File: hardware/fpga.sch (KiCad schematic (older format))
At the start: 18 parts

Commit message: more work on tdr schematic
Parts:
- removed U?: pkl_memory:W25Q, symbol icebreaker-cache:pkl_memory_W25Q
- added C? (x2): 100 nF, symbol Device:C_Small
- added C?: 10 nF, symbol Device:C_Small
- added C?: 2.2 uF, symbol Device:C_Small
- added C?: 100 pF, symbol Device:C_Small
- added L?: L_Small, symbol Device:L_Small
- U? (x4): symbol synth_lib:ICE40UP5K-SG48ITR -> tdr-rescue:ICE40UP5K-SG48ITR-synth_lib
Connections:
- net labels added: DELAY_SCLK, DELAY_SDIN, DELAY_SLOAD, DELAY_~EN, SEL0, SEL1, TRIG_DAC_CS, TRIG_DAC_SCK, TRIG_DAC_SDI
- net labels removed: D0_PULSE, D0_SAMPLE, D1_PULSE, D1_SAMPLE, D2_PULSE, D2_SAMPLE, D3_PULSE, D3_SAMPLE, D4_PULSE, D4_SAMPLE, D5_PULSE, D5_SAMPLE, D6_PULSE, D6_SAMPLE, D7_PULSE, D7_SAMPLE, D8_PULSE, D8_SAMPLE, D9_PULSE, D9_SAMPLE, PULSE_LATCH, SAMPLE_LATCH, ~PULSE_EN, ~SAMPLE_EN
- wire segments 72 -> 94
- no-connect marks 7 -> 0
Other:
- note added: "TODO: add digital test/ext control headers"
- note removed: "TODO: TERMINATE THESE"
- moved on the sheet: C?, R?

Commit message: work on tdr schematic..
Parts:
- removed C? (x5): 100 nF, symbol Device:C_Small
- removed C? (x3): 100 pF, symbol Device:C_Small
- removed C?: 10 uF, symbol Device:C_Small
- removed C? (x3): 10 nF, symbol Device:C_Small
- removed C? (x2): 1 uF, symbol Device:C_Small
- removed C?: 2.2 uF, symbol Device:C_Small
- removed L?: L_Small, symbol Device:L_Small
- removed R? (x3): R_Small, symbol Device:R_Small
- removed U? (x4): ICE40UP5K-SG48ITR, Package_DFN_QFN:QFN-48-1EP_7x7mm_P0.5mm_EP5.6x5.6mm, symbol tdr-rescue:ICE40UP5K-SG48ITR-synth_lib
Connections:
- net labels added: DAC_CS, DAC_SCK, DAC_SDI
- net labels removed: +1V2, +2V5, +3.3VP, +3V3, D0_DAC, D1_DAC, D2_DAC, D3_DAC, D4_DAC, D5_DAC, D6_DAC, D7_DAC, D8_DAC, D9_DAC, DAC_SLEEP, FLASH_~HLD~|~RST, FLASH_~WP, GND, ICE_DONE, ICE_SCK, ICE_SI, ICE_SO, ICE_SS, ICE_~RESET, TRIG_DAC_CS, TRIG_DAC_SCK, TRIG_DAC_SDI, UART_RX, UART_TX
- wire segments 94 -> 0
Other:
- note removed: "TODO: OPEN COLLECTOR!"

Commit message: work on schematic..
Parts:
- added C801, C803, C805, C807, C811, C812, C813, C814, C815, C816, C817, C818, C819, C820, C821, C822: 33 pF, Capacitors_SMD:C_0402, symbol Device:C_Small
- added C802, C806: 1 uF, Capacitors_SMD:C_0603, symbol Device:C_Small
- added C804, C808: 10 nF, Capacitors_SMD:C_0402, symbol Device:C_Small
- added C809, C810: C_Small, Capacitors_SMD:C_0402, symbol Device:C_Small
- added J801, J802: Conn_02x06_Odd_Even, Pin_Headers:Pin_Header_Angled_2x06, symbol Connector_Generic:Conn_02x06_Odd_Even
- added L801, L802: L_Small, Resistors_SMD:R_0402, symbol Device:L_Small
- added RN801, RN802, RN803, RN804, RN805, RN806, RN807: 22, Resistors_SMD:R_Array_Convex_4x0402, symbol Device:R_Pack04
- added TP801, TP802, TP803: TestPoint, vna_footprints:TP07R, symbol Connector:TestPoint
- added U801, U802: 74HC244, Housings_SSOP:TSSOP-20_4.4x6.5mm_Pitch0.65mm, symbol 74xx:74HC244
- added U803: 74xx1G14, TO_SOT_Packages_SMD:SOT-23-5, symbol 74xx1g14:74xx1G14
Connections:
- net DAC_CS: now also C821.1, RN807.7 (R2.2)
- net DAC_SCK: now also C819.1, RN807.6 (R3.2)
- net DAC_SDI: now also C817.1, RN807.5 (R4.2)
- net DELAY_SCLK: now also C816.1, RN806.6 (R3.2)
- net DELAY_SDIN: now also C818.1, RN806.7 (R2.2)
- net DELAY_SLOAD: now also C811.1, RN803.5 (R4.2)
- net DELAY_~EN: now also C815.1, RN806.5 (R4.2)
- net FPGA_CLK: now also C801.1, RN801.8 (R1.2)
- net REF_CLK_SEL: now also C812.1, RN803.6 (R3.2)
- net SEL0: now also C813.1, RN803.7 (R2.2)
- net SEL1: now also C814.1, RN803.8 (R1.2)
- new net: U801.1 (1OE), U802.1 (1OE), U802.19 (2OE), U803.4 (Y)
- new net: RN805.5 (R4.2), U802.11 (2A3)
- new net: RN807.4 (R4.1), U802.12 (1Y3)
- new net: RN805.6 (R3.2), U802.13 (2A2)
- new net: RN807.3 (R3.1), U802.14 (1Y2)
- new net: RN805.7 (R2.2), U802.15 (2A1)
- new net: RN807.2 (R2.1), U802.16 (1Y1)
- new net: RN805.8 (R1.2), U802.17 (2A0)
- new net: RN807.1 (R1.1), U802.18 (1Y0)
- new net: RN804.8 (R1.2), U802.2 (1A0)
- new net: C806.1, C808.1, L802.2, U802.20 (VCC)
- new net: RN803.1 (R1.1), U802.3 (2Y0)
- new net: RN804.7 (R2.2), U802.4 (1A1)
- new net: RN803.2 (R2.1), U802.5 (2Y1)
- new net: RN804.6 (R3.2), U802.6 (1A2)
- new net: RN803.3 (R3.1), U802.7 (2Y2)
- new net: RN804.5 (R4.2), U802.8 (1A3)
- new net: RN803.4 (R4.1), U802.9 (2Y3)
- new net: J801.1 (Pin_1), RN801.1 (R1.1)
- new net: J801.3 (Pin_3), RN801.2 (R2.1)
- new net: J801.5 (Pin_5), RN801.3 (R3.1)
- new net: J801.7 (Pin_7), RN801.4 (R4.1)
- new net: C807.1, RN801.5 (R4.2), TP803.1
- new net: C805.1, RN801.6 (R3.2), TP802.1
- new net: C803.1, RN801.7 (R2.2), TP801.1
- new net: RN806.4 (R4.1), U801.12 (1Y3)
- new net: RN806.3 (R3.1), U801.14 (1Y2)
- new net: RN806.2 (R2.1), U801.16 (1Y1)
- new net: RN806.1 (R1.1), U801.18 (1Y0)
- new net: C802.1, C804.1, L801.2, U801.20 (VCC)
- new net: J802.7 (Pin_7), RN802.5 (R4.2)
- new net: J802.5 (Pin_5), RN802.6 (R3.2)
- new net: J802.3 (Pin_3), RN802.7 (R2.2)
- new net: J802.1 (Pin_1), RN802.8 (R1.2)
- new net: J801.2 (Pin_2), RN804.1 (R1.1)
- new net: J801.4 (Pin_4), RN804.2 (R2.1)
- new net: J801.6 (Pin_6), RN804.3 (R3.1)
- new net: J801.8 (Pin_8), RN804.4 (R4.1)
- new net: J802.2 (Pin_2), RN805.1 (R1.1)
- new net: J802.4 (Pin_4), RN805.2 (R2.1)
- new net: J802.6 (Pin_6), RN805.3 (R3.1)
- new net: J802.8 (Pin_8), RN805.4 (R4.1)
- new net +3.3VP: C809.1, C810.1, J801.11 (Pin_11), J801.12 (Pin_12), J802.11 (Pin_11), J802.12 (Pin_12)
- new net +3V3: L801.1, L802.1, U801.19 (2OE), U803.5 (Vcc)
- new net COMPARATOR_OUTPUT: U801.2 (1A0)
- new net DAC_~CLR: C822.1, RN807.8 (R1.2)
- new net EXT_COMP_OUT: C820.1, RN802.1 (R1.1), RN806.8 (R1.2)
- new net EXT_DELAY_SCK: RN802.4 (R4.1), U801.8 (1A3)
- new net EXT_DELAY_SDIN: RN802.2 (R2.1), U801.4 (1A1)
- new net EXT_DELAY_~EN: RN802.3 (R3.1), U801.6 (1A2)
- new net GND: C801.2, C802.2, C803.2, C804.2, C805.2, C806.2, C807.2, C808.2, C809.2, C810.2, C811.2, C812.2, C813.2, C814.2, C815.2, C816.2, C817.2, C818.2, C819.2, C820.2, C821.2, C822.2, J801.10 (Pin_10), J801.9 (Pin_9), J802.10 (Pin_10), J802.9 (Pin_9), U801.10 (GND), U801.11 (2A3), U801.13 (2A2), U801.15 (2A1), U801.17 (2A0), U802.10 (GND), U803.3 (GND)
- new net PGOOD_3V3: U803.2 (A)
- no-connect marks 0 -> 4
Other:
- note added: "10.16 mm pad center to pad center"
- note added: "7 8 9 0 1 2\n1 2 3 4 5 6"
- note added: "TODO: BUFFER DIGITAL LINES VIA PGOOD SIGNAL OF DIGITAL CHIPS"
- note removed: "TODO: add digital test/ext control headers"

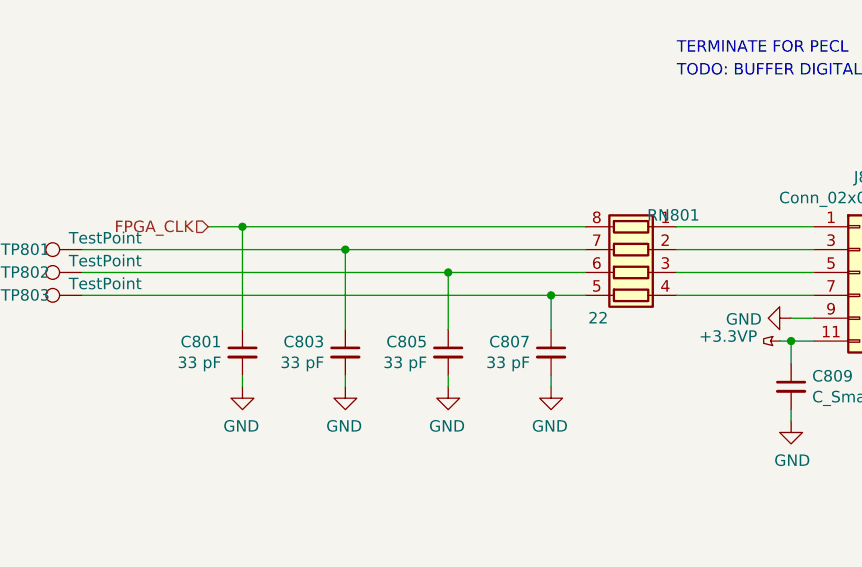
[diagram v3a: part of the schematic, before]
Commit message: work on tdr component placement
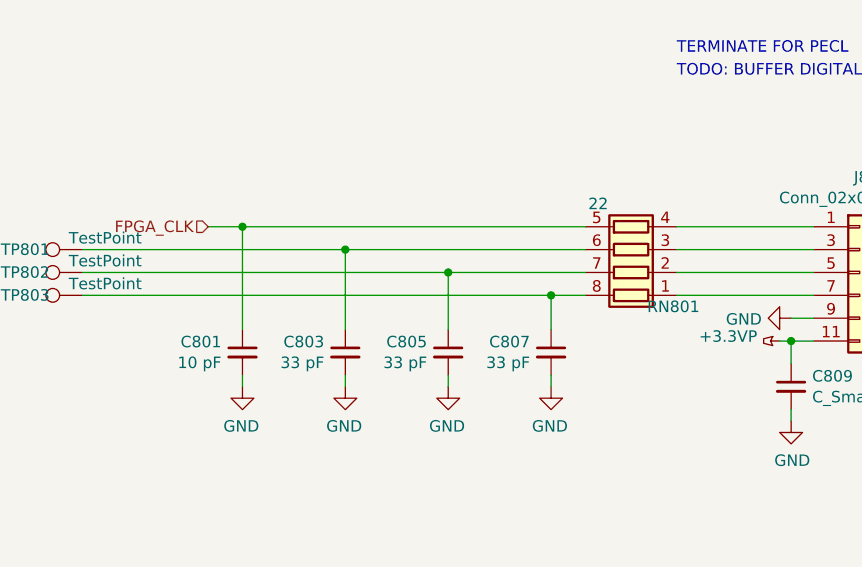
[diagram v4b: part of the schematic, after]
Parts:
- C801: value 33 pF -> 10 pF
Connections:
- net FPGA_CLK: now also RN801.5 (R4.2); no longer RN801.8 (R1.2)
- net at RN801.1 (R1.1): now also J801.7 (Pin_7); no longer J801.1 (Pin_1)
- net at RN801.2 (R2.1): now also J801.5 (Pin_5); no longer J801.3 (Pin_3)
- net at RN801.3 (R3.1): now also J801.3 (Pin_3); no longer J801.5 (Pin_5)
- net at RN801.4 (R4.1): now also J801.1 (Pin_1); no longer J801.7 (Pin_7)
- net at C807.1, TP803.1: now also RN801.8 (R1.2); no longer RN801.5 (R4.2)
- net at C805.1, TP802.1: now also RN801.7 (R2.2); no longer RN801.6 (R3.2)
- net at C803.1, TP801.1: now also RN801.6 (R3.2); no longer RN801.7 (R2.2)
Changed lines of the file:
@@
 L Device:R_Pack04 RN?
 U 1 1 5C12A862
-P 4500 2450
+P 4500 2350
 AR Path="/5BC6A656/5C12A862" Ref="RN?"  Part="1"
 AR Path="/5BC64E97/5C12A862" Ref="RN?"  Part="1"
 AR Path="/5BC3F67C/5C12A862" Ref="RN801"  Part="1"
-F 0 "RN801" V 4250 2150 50  0000 L CNN
-F 1 "22" V 4700 2550 50  0000 L CNN
-F 2 "Resistors_SMD:R_Array_Convex_4x0402" V 4775 2450 50  0001 C CNN
-F 3 "~" H 4500 2450 50  0001 C CNN
-	1    4500 2450
-	0    -1   1    0
+F 0 "RN801" V 4250 2050 50  0000 L CNN
+F 1 "22" V 4700 2450 50  0000 L CNN
+F 2 "Resistors_SMD:R_Array_Convex_4x0402" V 4775 2350 50  0001 C CNN
+F 3 "~" H 4500 2350 50  0001 C CNN
+	1    4500 2350
+	0    -1   -1   0
 $EndComp
 $Comp
@@
 P 2800 2800
 F 0 "C801" H 2892 2846 50  0000 L CNN
-F 1 "33 pF" H 2892 2755 50  0000 L CNN
+F 1 "10 pF" H 2892 2755 50  0000 L CNN
 F 2 "Capacitors_SMD:C_0402" H 2800 2800 50  0001 C CNN
 F 3 "~" H 2800 2800 50  0001 C CNN

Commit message: finished first pass component placement and drc setup, swapped digital pins for easier routing
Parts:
- removed J801, J802: Conn_02x06_Odd_Even, Pin_Headers:Pin_Header_Angled_2x06, symbol Connector_Generic:Conn_02x06_Odd_Even
- added J801, J802: Conn_02x06_Counter_Clockwise, Pin_Headers:Pin_Header_Angled_2x06, symbol Connector_Generic:Conn_02x06_Counter_Clockwise
- C809, C810: value C_Small -> 100 nF
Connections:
- net +3.3VP: now also J801.1 (Pin_1), J801.2 (Pin_2), J802.1 (Pin_1), J802.2 (Pin_2)
- net DELAY_SLOAD: now also RN803.8 (R1.2); no longer RN803.5 (R4.2)
- net EXT_COMP_OUT: now also J802.5 (Pin_5); no longer RN802.1 (R1.1)
- net EXT_DELAY_SCK: now also RN802.1 (R1.1); no longer RN802.4 (R4.1)
- net EXT_DELAY_SDIN: now also RN802.3 (R3.1); no longer RN802.2 (R2.1)
- net EXT_DELAY_~EN: now also RN802.2 (R2.1); no longer RN802.3 (R3.1)
- net FPGA_CLK: now also RN801.8 (R1.2); no longer RN801.5 (R4.2)
- net GND: now also J801.3 (Pin_3), J801.4 (Pin_4), J802.3 (Pin_3), J802.4 (Pin_4)
- net REF_CLK_SEL: now also RN803.7 (R2.2); no longer RN803.6 (R3.2)
- net SEL0: now also RN803.6 (R3.2); no longer RN803.7 (R2.2)
- net SEL1: now also RN803.5 (R4.2); no longer RN803.8 (R1.2)
- net at U802.3 (2Y0): now also RN803.4 (R4.1); no longer RN803.1 (R1.1)
- net at U802.5 (2Y1): now also RN803.3 (R3.1); no longer RN803.2 (R2.1)
- net at U802.7 (2Y2): now also RN803.2 (R2.1); no longer RN803.3 (R3.1)
- net at U802.9 (2Y3): now also RN803.1 (R1.1); no longer RN803.4 (R4.1)
- net at RN801.1 (R1.1): now also J801.12 (Pin_12)
- net at RN801.2 (R2.1): now also J801.11 (Pin_11)
- net at RN801.3 (R3.1): now also J801.10 (Pin_10)
- net at RN801.4 (R4.1): now also J801.9 (Pin_9)
- net at C803.1, TP801.1: now also RN801.7 (R2.2); no longer RN801.6 (R3.2)
- net at C805.1, TP802.1: now also RN801.6 (R3.2); no longer RN801.7 (R2.2)
- net at C807.1, TP803.1: now also RN801.5 (R4.2); no longer RN801.8 (R1.2)
- net at RN802.6 (R3.2): now also J802.8 (Pin_8)
- net at RN802.7 (R2.2): now also J802.7 (Pin_7)
- net at RN802.8 (R1.2): now also J802.6 (Pin_6)
- net at RN804.1 (R1.1): now also J801.8 (Pin_8)
- net at RN804.2 (R2.1): now also J801.7 (Pin_7)
- net at RN804.3 (R3.1): now also J801.6 (Pin_6)
- net at RN804.4 (R4.1): now also J801.5 (Pin_5)
- net at RN805.1 (R1.1): now also J802.12 (Pin_12)
- net at RN805.2 (R2.1): now also J802.11 (Pin_11)
- net at RN805.3 (R3.1): now also J802.10 (Pin_10)
- net at RN805.4 (R4.1): now also J802.9 (Pin_9)
- no-connect marks 4 -> 6
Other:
- note removed: "TODO: BUFFER DIGITAL LINES VIA PGOOD SIGNAL OF DIGITAL CHIPS"
- moved on the sheet: C801, C803, C805, C807, C809, C810, RN801, RN802, TP801, TP802, TP803

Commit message: layout of low speed digital traces
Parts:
- C801: value 10 pF -> 33 pF
- C807: value 33 pF -> 10 pF
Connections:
- net FPGA_CLK: now also C807.1, RN801.5 (R4.2); no longer C801.1, RN801.8 (R1.2)
- net at U802.2 (1A0): now also RN804.5 (R4.2); no longer RN804.8 (R1.2)
- net at U802.4 (1A1): now also RN804.6 (R3.2); no longer RN804.7 (R2.2)
- net at U802.6 (1A2): now also RN804.7 (R2.2); no longer RN804.6 (R3.2)
- net at U802.8 (1A3): now also RN804.8 (R1.2); no longer RN804.5 (R4.2)
- new net: C801.1, RN801.8 (R1.2), TP803.1
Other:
- moved on the sheet: TP803
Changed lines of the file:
@@
 Text HLabel 12200 4600 2    50   Output ~ 0
 REF_CLK_SEL
-Text HLabel 1850 1850 0    50   Input ~ 0
+Text HLabel 1300 2150 0    50   Input ~ 0
 FPGA_CLK
 Text Notes 4700 1500 0    50   ~ 0
@@
 P 3350 2400
 F 0 "C807" H 3442 2446 50  0000 L CNN
-F 1 "33 pF" H 3442 2355 50  0000 L CNN
+F 1 "10 pF" H 3442 2355 50  0000 L CNN
 F 2 "Capacitors_SMD:C_0402" H 3350 2400 50  0001 C CNN
 F 3 "~" H 3350 2400 50  0001 C CNN
@@
 P 2000 2400
 F 0 "C801" H 2092 2446 50  0000 L CNN
-F 1 "10 pF" H 2092 2355 50  0000 L CNN
+F 1 "33 pF" H 2092 2355 50  0000 L CNN
 F 2 "Capacitors_SMD:C_0402" H 2000 2400 50  0001 C CNN
 F 3 "~" H 2000 2400 50  0001 C CNN
@@
 	2000 1850 2000 2300
 Connection ~ 2000 1850
-Wire Wire Line
-	2000 1850 1850 1850
 $Comp
 L power:GND #PWR0322
@@
 DAC_~CLR
 Wire Wire Line
-	6700 4700 8600 4700
-Wire Wire Line
-	6700 4600 8600 4600
-Wire Wire Line
-	6700 4500 8600 4500
-Wire Wire Line
-	6700 4400 8600 4400
-Wire Wire Line
 	7450 4300 8600 4300
 Wire Wire Line
@@
 L Connector:TestPoint TP803
 U 1 1 5C2CEB4F
-P 1300 2150
-F 0 "TP803" V 1300 2400 50  0000 C CNN
-F 1 "TestPoint" V 1350 2050 50  0000 C CNN
-F 2 "vna_footprints:TP07R" H 1500 2150 50  0001 C CNN
-F 3 "~" H 1500 2150 50  0001 C CNN
-	1    1300 2150
+P 1300 1850
+F 0 "TP803" V 1300 2100 50  0000 C CNN
+F 1 "TestPoint" V 1350 1750 50  0000 C CNN
+F 2 "vna_footprints:TP07R" H 1500 1850 50  0001 C CNN
+F 3 "~" H 1500 1850 50  0001 C CNN
+	1    1300 1850
 	0    -1   -1   0
 $EndComp
@@
 	3900 2150 5000 2150
 Wire Wire Line
-	7450 2250 6700 2250
-Wire Wire Line
-	6700 2350 7550 2350
-Wire Wire Line
-	6700 2450 7650 2450
-Wire Wire Line
-	6700 2550 7750 2550
-Wire Wire Line
-	7450 4300 7450 2250
-Wire Wire Line
-	7550 2350 7550 4200
-Wire Wire Line
-	7650 2450 7650 4100
-Wire Wire Line
-	7750 2550 7750 4000
+	6700 4400 8600 4400
+Wire Wire Line
+	6700 4500 8600 4500
+Wire Wire Line
+	6700 4600 8600 4600
+Wire Wire Line
+	6700 4700 8600 4700
+Wire Wire Line
+	7750 2250 7750 4000
+Wire Wire Line
+	6700 2250 7750 2250
+Wire Wire Line
+	7650 4100 7650 2350
+Wire Wire Line
+	7650 2350 6700 2350
+Wire Wire Line
+	6700 2450 7550 2450
+Wire Wire Line
+	7550 2450 7550 4200
+Wire Wire Line
+	7450 4300 7450 2550
+Wire Wire Line
+	7450 2550 6700 2550
+Wire Wire Line
+	1300 1850 2000 1850
 $EndSCHEMATC

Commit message: first pass of layout complete
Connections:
- net DAC_CS: now also C818.1, RN806.7 (R2.2); no longer C821.1, RN807.7 (R2.2)
- net DAC_SCK: now also C816.1, RN806.6 (R3.2); no longer C819.1, RN807.6 (R3.2)
- net DAC_SDI: now also C815.1, RN806.5 (R4.2); no longer C817.1, RN807.5 (R4.2)
- net DAC_~CLR: now also C817.1, RN807.5 (R4.2); no longer C822.1, RN807.8 (R1.2)
- net DELAY_SCLK: now also C819.1, RN807.6 (R3.2); no longer C816.1, RN806.6 (R3.2)
- net DELAY_SDIN: now also C821.1, RN807.7 (R2.2); no longer C818.1, RN806.7 (R2.2)
- net DELAY_~EN: now also C822.1, RN807.8 (R1.2); no longer C815.1, RN806.5 (R4.2)
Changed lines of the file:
@@
 Comment4 ""
 $EndDescr
-Text HLabel 12250 3350 2    50   Output ~ 0
+Text HLabel 12250 6800 2    50   Output ~ 0
 DAC_CS
 Text HLabel 12200 4600 2    50   Output ~ 0
@@
 Text HLabel 12200 4500 2    50   Output ~ 0
 SEL0
-Text HLabel 12250 3450 2    50   Output ~ 0
+Text HLabel 12250 6900 2    50   Output ~ 0
 DAC_SCK
-Text HLabel 12250 3550 2    50   Output ~ 0
+Text HLabel 12250 7000 2    50   Output ~ 0
 DAC_SDI
 $Comp
@@
 Wire Wire Line
 	9750 3250 10200 3250
-Text HLabel 12250 3250 2    50   Output ~ 0
+Text HLabel 12250 3550 2    50   Output ~ 0
 DAC_~CLR
 Wire Wire Line
@@
 Wire Wire Line
 	9750 6700 10200 6700
-Text HLabel 12250 7000 2    50   Output ~ 0
+Text HLabel 12250 3250 2    50   Output ~ 0
 DELAY_~EN
-Text HLabel 12250 6800 2    50   Input ~ 0
+Text HLabel 12250 3350 2    50   Input ~ 0
 DELAY_SDIN
-Text HLabel 12250 6900 2    50   Input ~ 0
+Text HLabel 12250 3450 2    50   Input ~ 0
 DELAY_SCLK
 Text HLabel 8300 7450 0    50   Input ~ 0

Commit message: schematic cleanup, BOM consolidation
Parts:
- C802, C806: value 1 uF -> DNP
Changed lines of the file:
@@
 P 8350 3100
 F 0 "C806" H 8442 3146 50  0000 L CNN
-F 1 "1 uF" H 8442 3055 50  0000 L CNN
+F 1 "DNP" H 8442 3055 50  0000 L CNN
 F 2 "Capacitors_SMD:C_0603" H 8350 3100 50  0001 C CNN
 F 3 "~" H 8350 3100 50  0001 C CNN
@@
 P 8350 6550
 F 0 "C802" H 8442 6596 50  0000 L CNN
-F 1 "1 uF" H 8442 6505 50  0000 L CNN
+F 1 "DNP" H 8442 6505 50  0000 L CNN
 F 2 "Capacitors_SMD:C_0603" H 8350 6550 50  0001 C CNN
 F 3 "~" H 8350 6550 50  0001 C CNN
